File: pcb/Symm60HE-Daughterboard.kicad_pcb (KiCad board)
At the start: 2 copper layers, 56 x 26 mm, 13 parts, among them J2 FFC_12P, J3 FFC_12P, SW1 TS-1187A, SW2 TS-1187A, U1 AT32F405RCT7, U2 USBLC6-2SC6, U3 TLV75733PDBV, U4 XC6206P332MR, Y1 12MHz

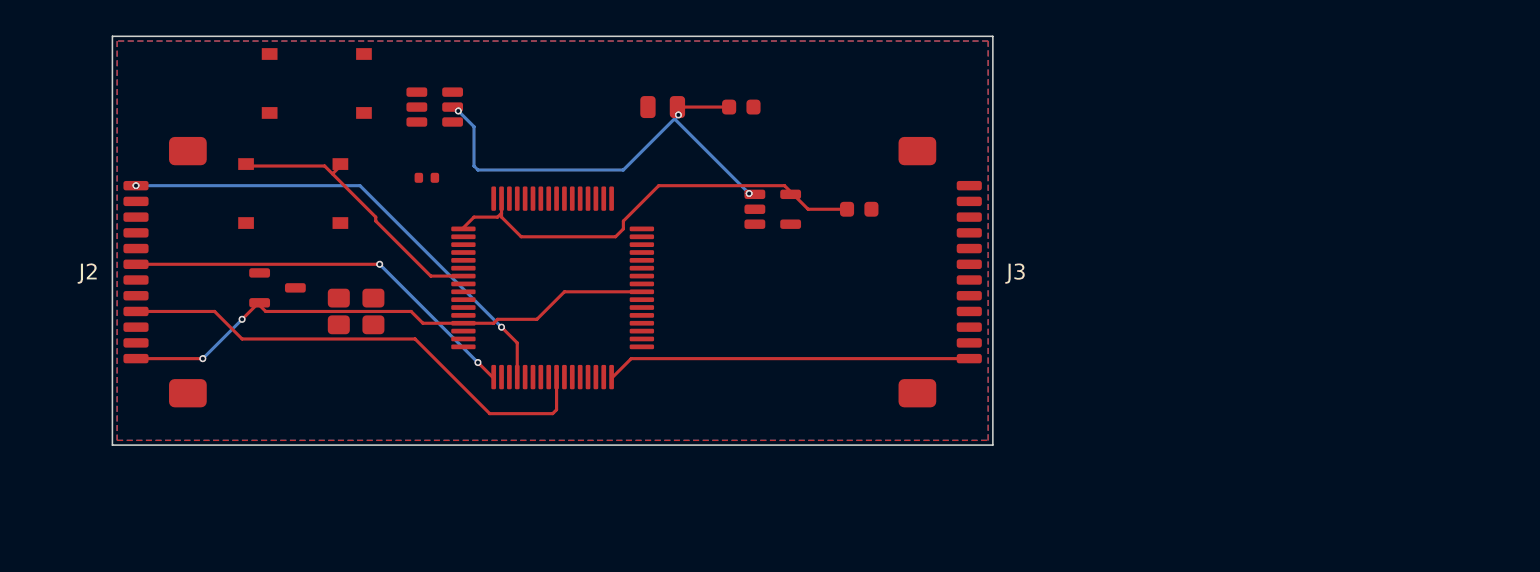
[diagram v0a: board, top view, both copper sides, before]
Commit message: Get the boards routing: SOIC muxes, FN40HE's pinout, a rail plane
Four changes, none of which touch what the circuit is made of.

SOIC-16 muxes.  FN40HE fits the SN74LV4051A in TSSOP-16, and every remaining
failure on the halves was an interior pin of one.  A 0.65 mm pitch leaves
0.25 mm between pads: no trace fits between them at any rule a fabricator
will take, so those pins could only ever escape by via through a gap their
neighbours already owned.  Same chip in SOIC-16 -- SN74LV4051AD -- has
1.27 mm pitch and 0.67 mm between pads, which a 0.2 mm trace clears with
0.15 mm either side.  It costs about 30 mm2 a package on boards that have
room under the keycaps, and it hand solders.

The MCU pin assignment is FN40HE's again, read off its board: crystal on
5/6, reset on 7, the mux selects on 9/10/11, the analog rail on 13, the
eight multiplexed inputs on 17 and 20-26, USB and its reference resistor on
33/34/35, SWD on 46/49/55, boot on 60.  The previous commit had moved those
around to suit the layout, which is backwards -- most of them are fixed in
silicon.  The parts move instead.  NOTICE.md is corrected accordingly.

The analog rail is a pour, not a net.  It reaches 75 pads on the left half;
routed as traces it is a spanning tree that gets there first and walls off
the three select lines, which have one shape that works.  F.Cu carries it
instead -- the halves have no components on the front -- and each rail pad
taps it through a via of its own.  That is FN40HE's +3.3VA zone, on the
other side because our board is populated the other way up.  B.Cu stays the
GND pour, so neither rail is routed.

And the one that mattered most: a pad's list of ways to be met had the bare
pad centre first.  Meeting a pad in its middle lets the maze leave sideways,
which on a 0.5 mm pitch package crosses the neighbouring pin, so all twelve
of those candidates were found and then thrown out by the clearance check --
exhausting the per-pad budget before the escapes along the pad's own a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
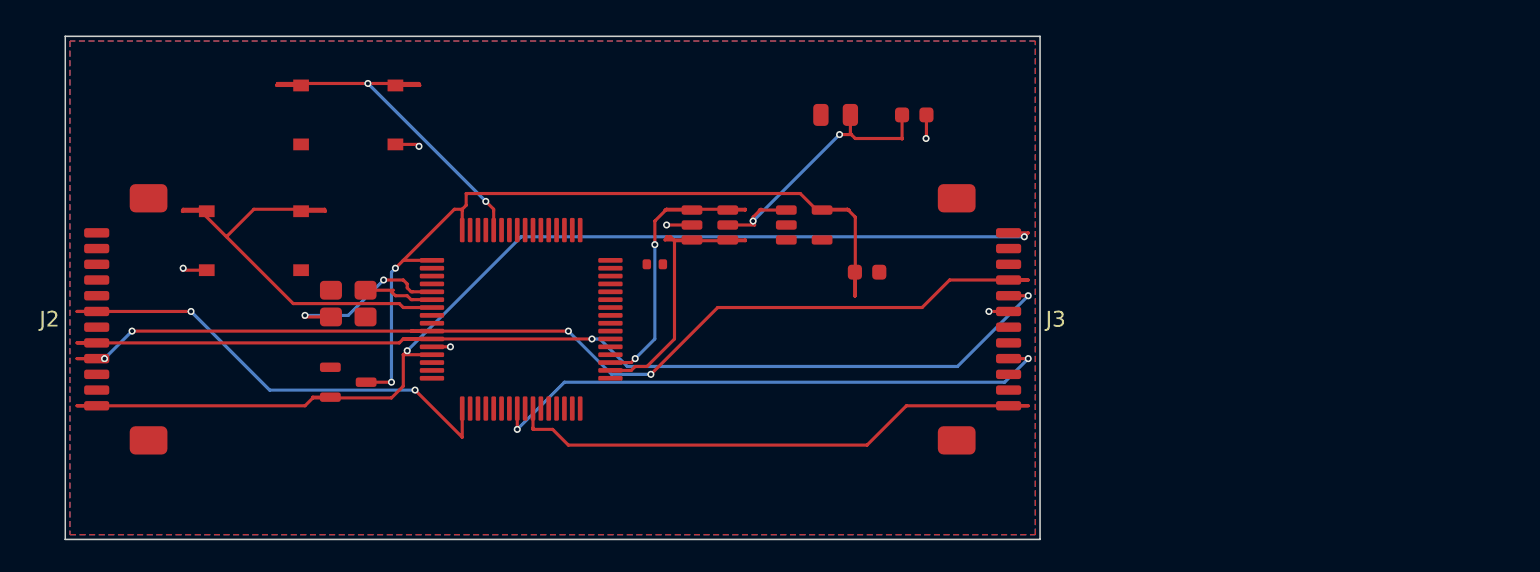
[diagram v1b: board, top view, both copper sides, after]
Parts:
- moved U2 19.0 mm to (161.2, 4.24)
- moved R1 15.5 mm to (157.7, 6.74)
- moved C1 11.0 mm to (174.2, -2.76)
- moved F1 11.0 mm to (169.2, -2.76)
- moved U4 7.50 mm to (138.2, 14.2)
- moved C2 4.03 mm to (171.2, 7.24)
- moved J2 3.91 mm to (124.2, 10.2)
- moved J3 3.91 mm to (178.2, 10.2)
- moved SW2 3.91 mm to (132.2, 5.24)
- moved SW1 2.83 mm to (138.2, -2.76)
- moved U1 2.83 mm to (149.2, 10.2)
- moved U3 2.24 mm to (167.2, 4.24)
- moved Y1 0.71 mm to (138.2, 9.24)
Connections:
- U1 pad 10: (no net) -> MUX_A1
- U1 pad 11: (no net) -> MUX_A2
- U1 pad 18: ADC_L2 -> (no net)
- U1 pad 19: ADC_L3 -> (no net)
- U1 pad 20: ADC_L4 -> ADC_L2
- U1 pad 21: (no net) -> ADC_L3
- U1 pad 22: GND -> ADC_L4
- U1 pad 23: (no net) -> ADC_R1
- U1 pad 24: MUX_A0 -> ADC_R2
- U1 pad 25: MUX_A1 -> ADC_R3
- U1 pad 26: MUX_A2 -> ADC_R4
- U1 pad 28: GND -> (no net)
- U1 pad 29: ADC_R1 -> (no net)
- U1 pad 30: ADC_R2 -> (no net)
- U1 pad 31: ADC_R3 -> GND
- U1 pad 32: ADC_R4 -> (no net)
- U1 pad 33: (no net) -> USB_R
- U1 pad 34: (no net) -> USB_DM
- U1 pad 35: (no net) -> USB_DP
- U1 pad 40: +3V3A -> (no net)
- U1 pad 44: GND -> (no net)
- U1 pad 46: (no net) -> SWDIO
- U1 pad 51: SWDIO -> (no net)
- U1 pad 53: SWO -> (no net)
- U1 pad 55: (no net) -> SWO
- U1 pad 56: USB_DM -> (no net)
- U1 pad 57: USB_DP -> (no net)
- U1 pad 58: USB_R -> (no net)
- U1 pad 63: +3V3D -> GND
- U1 pad 64: (no net) -> +3V3D
- U1 pad 9: (no net) -> MUX_A0
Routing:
- net MUX_A2: track 0.07 -> 67.5 mm, vias 0 -> 2
- net MUX_A1: track 31.6 -> 68.7 mm, vias 0 -> 4
- net ADC_R2: track 0.07 -> 36.9 mm, vias 0 -> 2
- net +3V3A: track 35.3 -> 71.7 mm
- net ADC_L4: track 30.7 -> 0.00 mm, vias 2 -> 0
- net BOOT0: track 0.07 -> 25.0 mm, vias 0 -> 2
- net +3V3D: track 29.2 -> 53.0 mm, vias 0 -> 2
- net USB_DP: track 0.07 -> 20.0 mm, vias 0 -> 2
- net USB_DM: track 0.07 -> 19.4 mm
- net ADC_R4: track 23.3 -> 35.5 mm
- net XTAL_IN: track 0.08 -> 11.4 mm, vias 0 -> 2
- net NRST: track 17.8 -> 28.8 mm
- net VBUS: track 29.9 -> 19.5 mm, vias 3 -> 2
- net GND: track 0.00 -> 9.27 mm, vias 0 -> 6
- net ADC_L1: track 25.8 -> 30.9 mm
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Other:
- board size 56 x 26 mm -> 62 x 32 mm

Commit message: Replace repo contents with current Symm60HE project folder
Adds firmware (libhmk), release fabrication outputs, pogo/neo PCB variants,
Fusion 360 case sources, and updated docs/tools.

Co-Authored-By: Claude Opus 5 <noreply@anthropic.com>
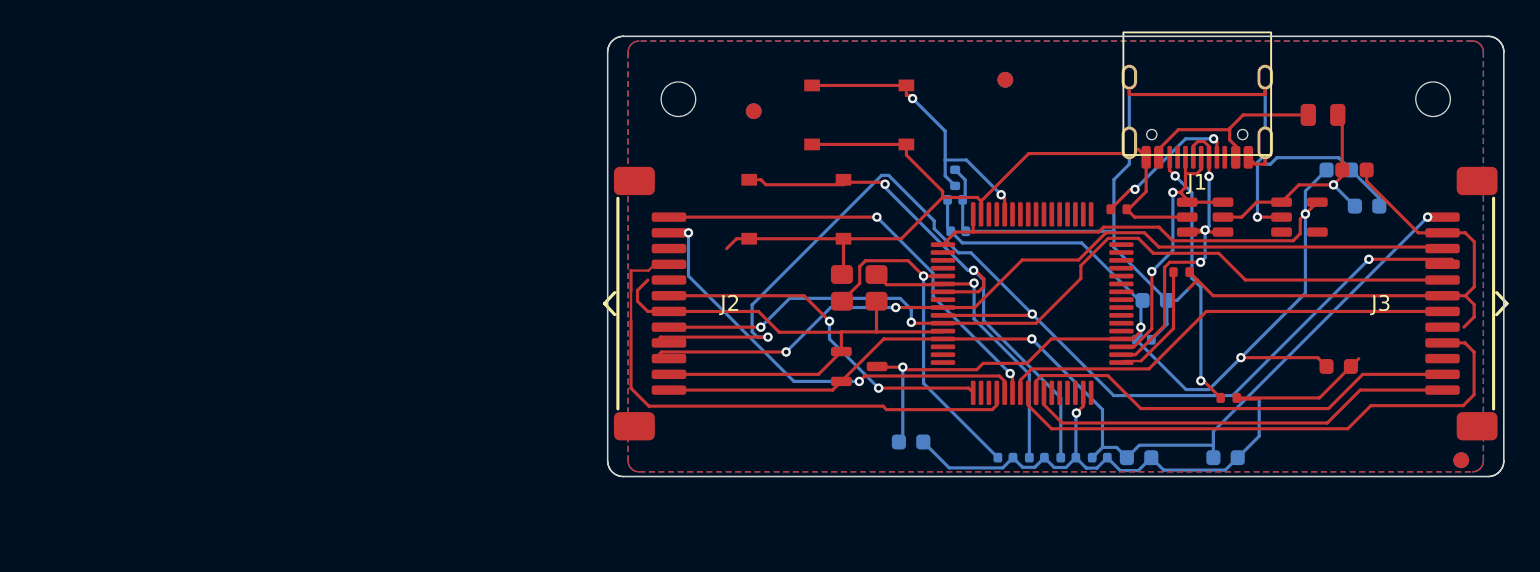
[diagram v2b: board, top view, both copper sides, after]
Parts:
- added C10: 1u, Symm60HE_Project:C148_C_0603_1608Metric, B.Cu at (188.5, 19.0)
- added C11: 100n, Symm60HE_Project:C1_C_0402_1005Metric, B.Cu at (184.0, 19.0)
- added C12: 2.2u, Symm60HE_Project:C148_C_0603_1608Metric, B.Cu at (203.0, 3.04)
- added C13: 2.2u, Symm60HE_Project:C148_C_0603_1608Metric, B.Cu at (201.2, 0.74)
- added C14: 2.2u, Symm60HE_Project:C148_C_0603_1608Metric, B.Cu at (174.0, 18.0)
- added C15: 2.2u, Symm60HE_Project:C148_C_0603_1608Metric, B.Cu at (194.0, 19.0)
- added C3: 30p, Symm60HE_Project:C1_C_0402_1005Metric, B.Cu at (180.0, 19.0)
- added C4: 30p, Symm60HE_Project:C1_C_0402_1005Metric, B.Cu at (182.0, 19.0)
- added C5: 100n, Symm60HE_Project:C1_C_0402_1005Metric, B.Cu at (177.0, 4.64)
- added C6: 100n, Symm60HE_Project:C1_C_0402_1005Metric, B.Cu at (188.8, 11.5)
- added C7: 100n, Symm60HE_Project:C1_C_0402_1005Metric, B.Cu at (176.8, 2.64)
- added C8: 10u, Symm60HE_Project:C148_C_0603_1608Metric, B.Cu at (189.5, 9.04)
- added C9: 100n, Symm60HE_Project:C1_C_0402_1005Metric, B.Cu at (186.0, 19.0)
- added FIDB1: FIDUCIAL_1MM_BCU, Symm60HE_Project:Fiducial_1mm_BCu, B.Cu at (164.0, -3.00)
- added FIDB2: FIDUCIAL_1MM_BCU, Symm60HE_Project:Fiducial_1mm_BCu, B.Cu at (180.0, -5.00)
- added FIDB3: FIDUCIAL_1MM_BCU, Symm60HE_Project:Fiducial_1mm_BCu, B.Cu at (209.0, 19.2)
- added FIDF1: FIDUCIAL_1MM_FCU, Symm60HE_Project:Fiducial_1mm_FCu, F.Cu at (164.0, -3.00)
- added FIDF2: FIDUCIAL_1MM_FCU, Symm60HE_Project:Fiducial_1mm_FCu, F.Cu at (180.0, -5.00)
- added FIDF3: FIDUCIAL_1MM_FCU, Symm60HE_Project:Fiducial_1mm_FCu, F.Cu at (209.0, 19.2)
- added J1: TYPE-C-31-M-12, Symm60HE_Project:USB_C_Receptacle_HRO_TYPE-C-31-M-12, F.Cu at (192.2, -4.11)
- added MHD1: M2_NPTH, Symm60HE_Project:MountingHole_2.2mm_M2_NPTH, F.Cu at (159.2, -3.76)
- added MHD2: M2_NPTH, Symm60HE_Project:MountingHole_2.2mm_M2_NPTH, F.Cu at (207.2, -3.76)
- added R2: 5.1k, Symm60HE_Project:R3_R_0402_1005Metric, F.Cu at (187.2, 3.24)
- added R3: 5.1k, Symm60HE_Project:R3_R_0402_1005Metric, F.Cu at (194.2, 15.2)
- added R4: 12k, Symm60HE_Project:R3_R_0402_1005Metric, B.Cu at (176.8, 1.24)
- moved SW2 34.6 mm to (166.7, 3.24)
- moved R1 33.5 mm to (191.2, 7.24)
- moved J2 33.3 mm to (157.5, 9.24), turned to -90 degrees
- moved U1 32.5 mm to (181.7, 9.24)
- moved U4 32.5 mm to (170.7, 13.2)
- moved Y1 32.5 mm to (170.7, 8.24)
- moved SW1 32.5 mm to (170.7, -2.76)
- moved U2 31.5 mm to (192.7, 3.74)
- moved U3 31.5 mm to (198.7, 3.74)
- moved F1 31.0 mm to (200.2, -2.76)
- moved J3 30.7 mm to (208.9, 9.24), turned to 90 degrees
- moved C2 30.6 mm to (201.2, 13.2)
- moved C1 28.2 mm to (202.2, 0.74)
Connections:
- J2 pad 1: +3V3A -> ADC_L4
- J2 pad 10: GND -> MUX_A0
- J2 pad 11: ADC_L3 -> GND
- J2 pad 12: ADC_L4 -> +3V3A
- J2 pad 2: GND -> ADC_L3
- J2 pad 3: MUX_A0 -> GND
- J2 pad 4: MUX_A1 -> ADC_L2
- J2 pad 5: MUX_A2 -> GND
- J2 pad 6: GND -> ADC_L1
- J2 pad 7: ADC_L1 -> GND
- J2 pad 8: GND -> MUX_A2
- J2 pad 9: ADC_L2 -> MUX_A1
- J3 pad 1: +3V3A -> ADC_R4
- J3 pad 10: GND -> MUX_A0
- J3 pad 11: ADC_R3 -> GND
- J3 pad 12: ADC_R4 -> +3V3A
- J3 pad 2: GND -> ADC_R3
- J3 pad 3: MUX_A0 -> GND
- J3 pad 4: MUX_A1 -> ADC_R2
- J3 pad 5: MUX_A2 -> GND
- J3 pad 6: GND -> ADC_R1
- J3 pad 7: ADC_R1 -> GND
- J3 pad 8: GND -> MUX_A2
- J3 pad 9: ADC_R2 -> MUX_A1
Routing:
- net GND: track 9.27 -> 234.3 mm, vias 6 -> 2
- net MUX_A0: track 0.00 -> 54.7 mm, vias 0 -> 2
- net +3V3D: track 53.0 -> 97.7 mm, vias 2 -> 4
- net ADC_L2: track 0.00 -> 33.9 mm
- net ADC_R1: track 0.00 -> 30.4 mm
- net ADC_R3: track 0.00 -> 29.4 mm
- net ADC_L4: track 0.00 -> 28.9 mm, vias 0 -> 2
- net ADC_L3: track 0.00 -> 28.8 mm, vias 0 -> 2
- net CC2: track 0.00 -> 16.8 mm, vias 0 -> 2
- net XTAL_OUT: track 4.67 -> 19.1 mm, vias 0 -> 1
- net VBUS_IN: track 0.00 -> 12.9 mm
- net MUX_A2: track 67.5 -> 56.7 mm
- net XTAL_IN: track 11.4 -> 22.0 mm, vias 2 -> 1
- net CC1: track 0.00 -> 9.67 mm, vias 0 -> 2
- net USB_R: track 0.00 -> 7.80 mm
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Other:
- board size 62 x 32 mm -> 57 x 28 mm
